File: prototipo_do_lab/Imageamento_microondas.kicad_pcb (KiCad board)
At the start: 4 copper layers, 200 x 150 mm, 121 parts, among them J1 0732511352, J10 0732511352, J11 TB0012-508-03GR, J12 0732511352, J13 0732511352, J2 0732511352, J3 0732511352, J4 0732511352, J5 0732511352, J6 0732511352, J7 0732511352, J8 0732511352, J9 0732511352, U1 SKY13373-460LF, U10 SKY13373-460LF, U11 SKY13373-460LF, U12 SKY13373-460LF, U13 SKY13373-460LF, U14 SKY13373-460LF, U15 SKY13373-460LF, U16 SKY13373-460LF, U17 ESP32-DEVKITC-32E, U18 MCP23016-I_SP, U2 SKY13373-460LF, U3 SKY13373-460LF, U4 SKY13373-460LF, U5 SKY13373-460LF, U6 SKY13373-460LF, U7 SKY13373-460LF, U8 SKY13373-460LF, U9 SKY13373-460LF

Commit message: backup version before new trace tracking
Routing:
- net /arbitragem/I2C_2: track 204.1 -> 0.00 mm
- net /arbitragem/I2C_1: track 165.8 -> 0.00 mm
- net /CE2_2: track 156.1 -> 19.2 mm, vias 1 -> 0
- net /CE1_1: track 144.6 -> 9.79 mm, vias 1 -> 0
- net /CE1_2: track 143.0 -> 8.31 mm, vias 1 -> 0
- net /CE2_1: track 153.8 -> 23.9 mm, vias 1 -> 0
- net /CA_14: track 137.4 -> 10.5 mm, vias 1 -> 0
- net /CA_13: track 142.1 -> 15.6 mm, vias 1 -> 0
- net /CE2_6: track 124.1 -> 8.33 mm, vias 1 -> 0
- net /CE2_5: track 125.1 -> 9.69 mm, vias 1 -> 0
- net /CA_4: track 125.0 -> 12.4 mm, vias 1 -> 0
- net /CA_3: track 123.3 -> 12.0 mm, vias 1 -> 0
- net /CE2_4: track 106.4 -> 8.32 mm, vias 1 -> 0
- net /CA_15: track 109.9 -> 12.0 mm, vias 1 -> 0
- net /CE2_3: track 107.7 -> 9.78 mm, vias 1 -> 0
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- removed copper zone on F.Cu, net GND
- removed copper zone on In1.Cu, net GND
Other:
- copper layers 4 -> 2

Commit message: before moving components
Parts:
- removed TP1, TP10, TP11, TP12, TP13, TP14, TP15, TP16, TP17, TP18, TP19, TP2, TP20, TP21, TP22, TP23, TP24, TP25, TP26, TP27, TP28, TP29, TP3, TP30, TP31, TP32, TP4, TP7, TP8, TP9: TestPoint, TestPoint:TestPoint_Pad_D1.5mm
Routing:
- net (no net): track 0.00 -> 355.1 mm
- net /R2_2: track 97.0 -> 0.00 mm
- net /R2_1: track 96.8 -> 0.00 mm
- net /R2_4: track 96.6 -> 0.00 mm
- net /R2_7: track 96.5 -> 0.00 mm
- net /R2_5: track 96.4 -> 0.00 mm
- net /R2_6: track 95.8 -> 0.00 mm
- net /R1_2: track 92.5 -> 0.00 mm
- net /R1_3: track 86.2 -> 0.00 mm
- net /R1_1: track 84.4 -> 0.00 mm
- net VDD: track 80.0 -> 0.00 mm
- net /segunda_camada_emissao/EXT_E: track 74.6 -> 0.00 mm
- net /E2_6: track 74.5 -> 0.00 mm
- net /E2_7: track 74.5 -> 0.00 mm
- net /E2_3: track 74.5 -> 0.00 mm
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
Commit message: track rounding partially made
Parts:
- removed TP5, TP6: TestPoint, TestPoint:TestPoint_Pad_D1.5mm
- moved C25 9.00 mm to (89.1, 101.2)
- moved C27 9.00 mm to (83.7, 104.9)
- moved C28 9.00 mm to (87.3, 104.9)
- moved C33 9.00 mm to (156.6, 90.5)
- moved C34 9.00 mm to (160.2, 90.5)
- moved C35 9.00 mm to (118.6, 90.3)
- moved C36 9.00 mm to (122.2, 90.3)
- moved C37 9.00 mm to (191.5, 105.0)
- moved C38 9.00 mm to (195.1, 105.0)
- moved C44 9.00 mm to (162.1, 86.8)
- moved C45 9.00 mm to (197.0, 101.2)
- moved C48 9.00 mm to (124.1, 86.6)
- moved R1 9.00 mm to (83.7, 108.3)
- moved R4 9.00 mm to (156.6, 93.9)
- moved R5 9.00 mm to (118.6, 93.7)
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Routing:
- net (no net): track 355.1 -> 1194.9 mm

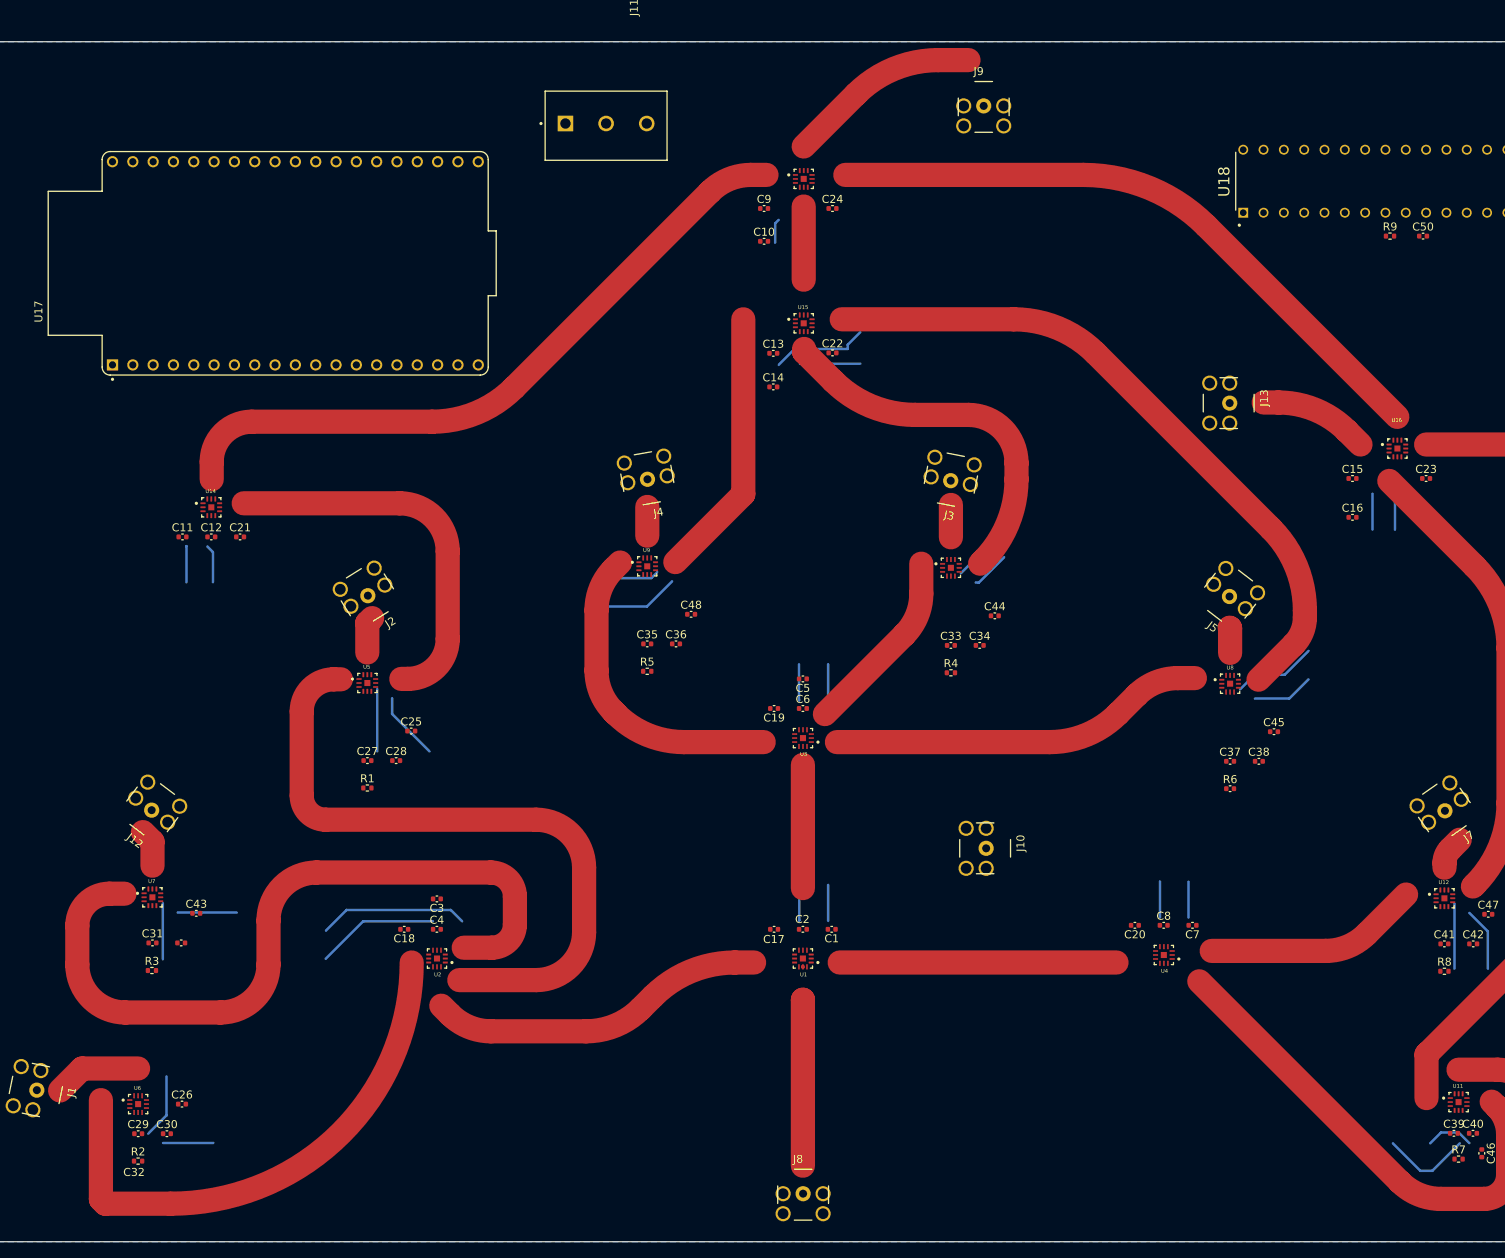
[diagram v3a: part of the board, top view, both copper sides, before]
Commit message: track rounding finished, still need validation
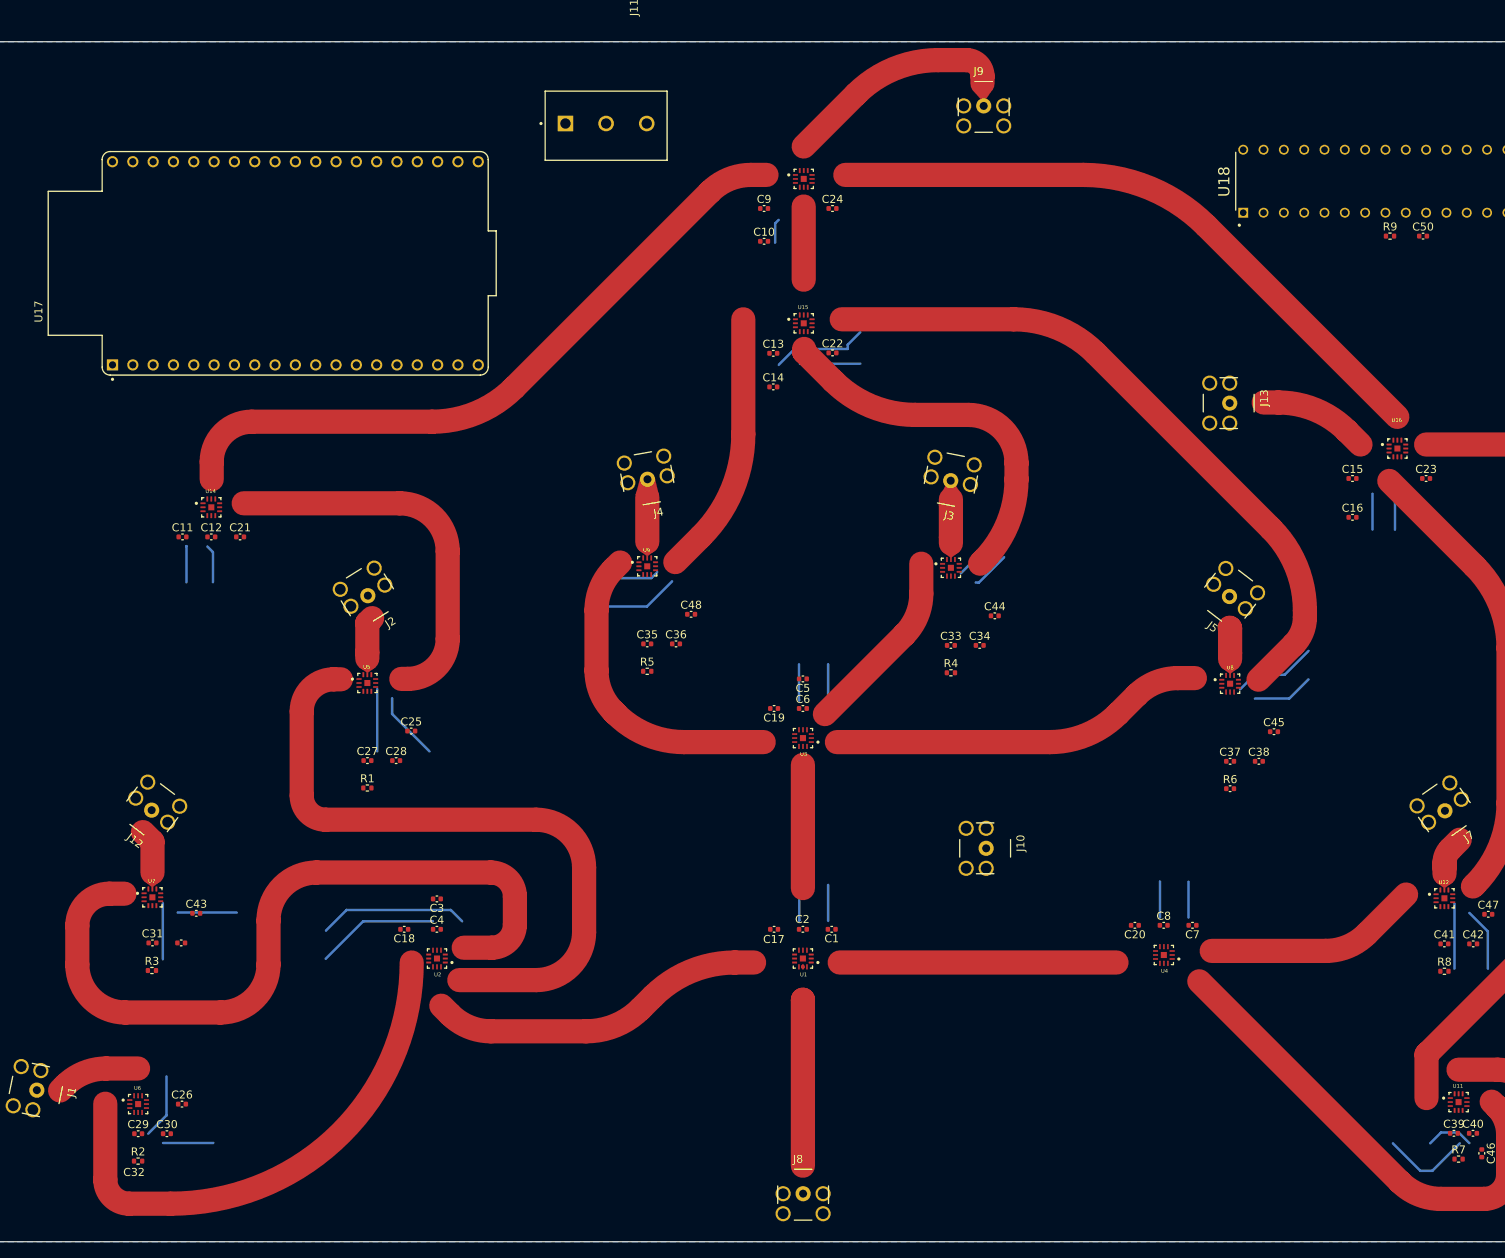
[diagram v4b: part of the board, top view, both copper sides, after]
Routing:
- net (no net): track 1194.9 -> 1143.0 mm
- net Net-(U13-RFC): track 0.00 -> 28.1 mm
- net Net-(U9-RFC): track 0.00 -> 5.55 mm
- net Net-(U7-RFC): track 0.00 -> 5.55 mm
- net Net-(U10-RFC): track 0.00 -> 5.49 mm
- net Net-(U5-RFC): track 0.00 -> 5.29 mm
- net Net-(U12-RFC): track 0.00 -> 4.93 mm
- net Net-(U8-RFC): track 0.00 -> 3.95 mm

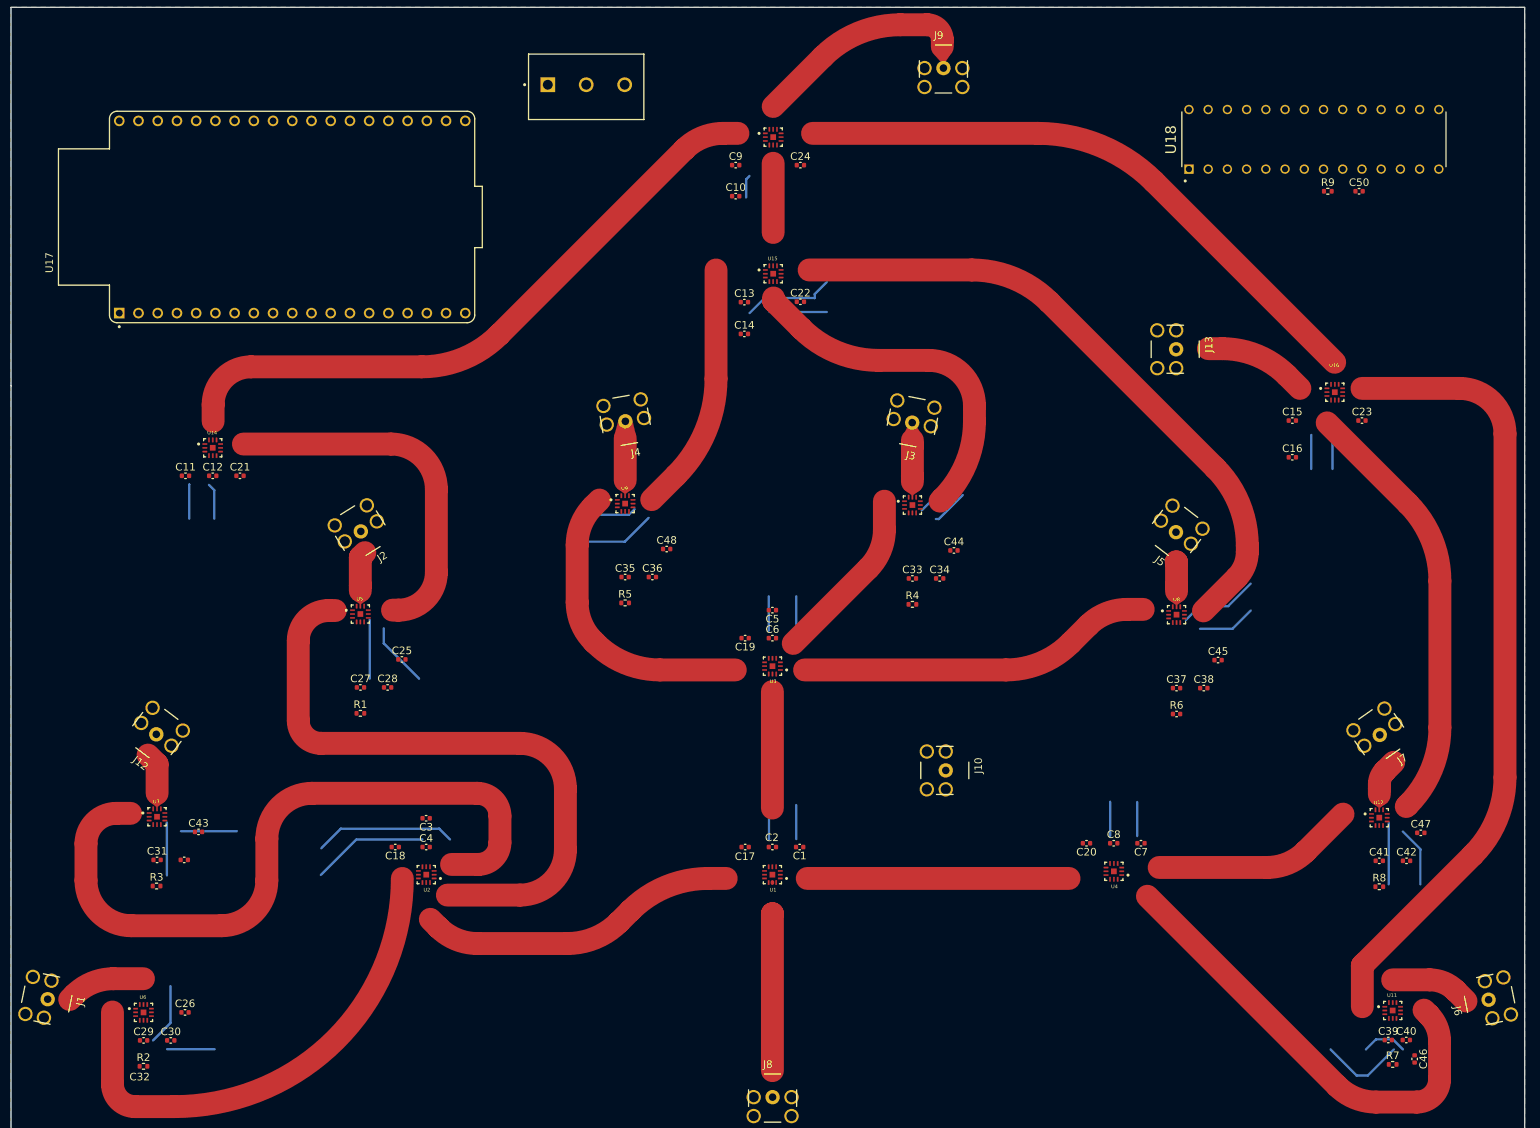
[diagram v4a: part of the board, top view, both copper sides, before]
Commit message: SMA connections finished
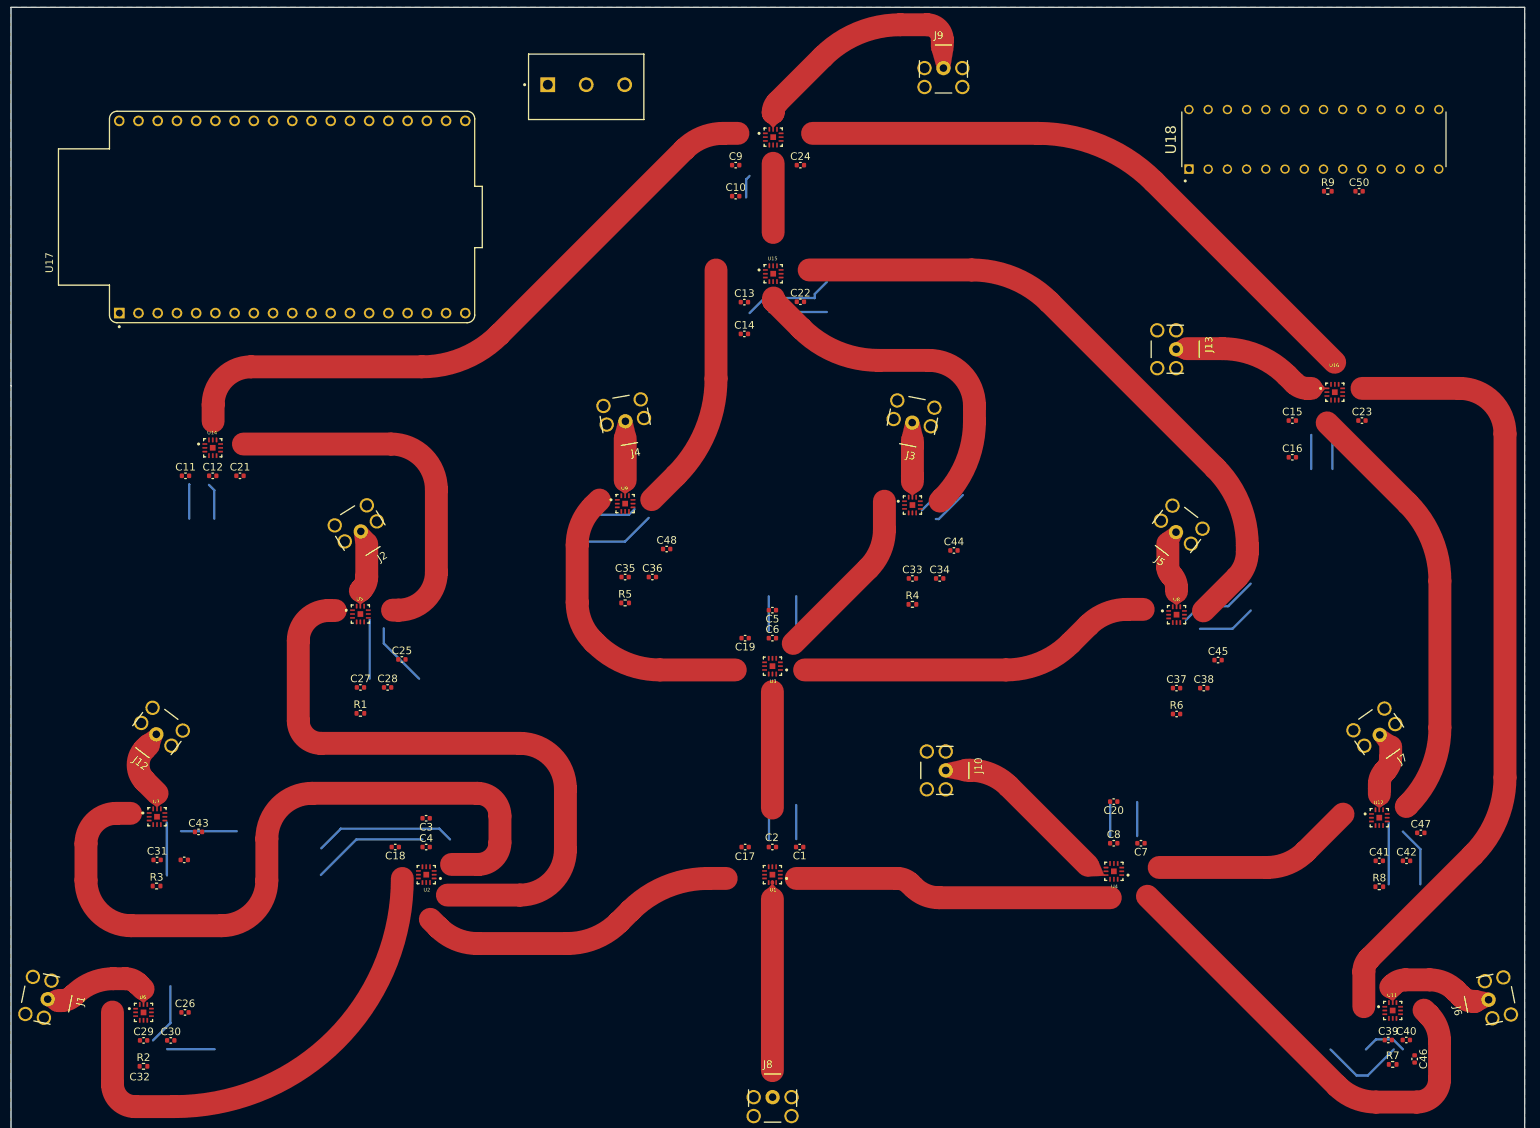
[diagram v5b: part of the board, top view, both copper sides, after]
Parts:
- moved C20 6.57 mm to (183.2, 120.0)
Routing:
- net (no net): track 1143.0 -> 1094.8 mm
- net Net-(U1-RFC): track 0.00 -> 22.7 mm
- net /segunda_camada_emissao/EXT_E: track 0.00 -> 20.9 mm
- net /segunda_camada_recepcao/EXT_R: track 0.00 -> 17.9 mm
- net Net-(U6-RFC): track 0.00 -> 12.4 mm
- net Net-(U11-RFC): track 0.00 -> 12.3 mm
- net Net-(U8-RFC): track 3.95 -> 6.63 mm
- net Net-(U7-RFC): track 5.55 -> 7.57 mm
- net Net-(U12-RFC): track 4.93 -> 6.69 mm
- net Net-(U5-RFC): track 5.29 -> 6.43 mm
- net Net-(U13-RFC): track 28.1 -> 28.8 mm

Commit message: rf tracking finished
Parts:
- moved C11 11.2 mm to (62.6, 88.0)
- moved C2 9.18 mm to (131.2, 120.0)
- moved C12 6.34 mm to (62.6, 83.0)
- moved C21 6.30 mm to (66.4, 83.0)
- moved C31 4.47 mm to (60.8, 129.7)
- moved C32 4.47 mm to (64.4, 129.7)
- moved C41 4.47 mm to (214.3, 129.8)
- moved C42 4.47 mm to (217.9, 129.8)
- moved C47 4.47 mm to (219.8, 126.1)
- moved R3 4.47 mm to (60.7, 133.1)
- moved R8 4.47 mm to (214.3, 133.2)
- moved C43 4.47 mm to (66.3, 126.0)
- moved C26 4.32 mm to (64.8, 148.1)
- moved C1 3.87 mm to (145.4, 124.8)
- moved C17 3.63 mm to (131.2, 124.5)
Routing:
- net (no net): track 1094.8 -> 84.4 mm
- net /R2_7: track 0.00 -> 105.2 mm
- net /R2_2: track 0.00 -> 98.0 mm
- net /R2_4: track 0.00 -> 89.8 mm
- net /R1_1: track 0.00 -> 88.0 mm
- net /R1_3: track 0.00 -> 83.4 mm
- net /E2_1: track 0.00 -> 83.3 mm
- net /E2_2: track 0.00 -> 68.4 mm
- net /E2_7: track 0.00 -> 64.4 mm
- net /R2_8: track 0.00 -> 61.6 mm
- net /R2_3: track 0.00 -> 55.6 mm
- net /R2_6: track 0.00 -> 52.6 mm
- net /E1_1: track 0.00 -> 50.9 mm
- net /R2_1: track 0.00 -> 50.2 mm
- net /E2_4: track 0.00 -> 49.6 mm
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
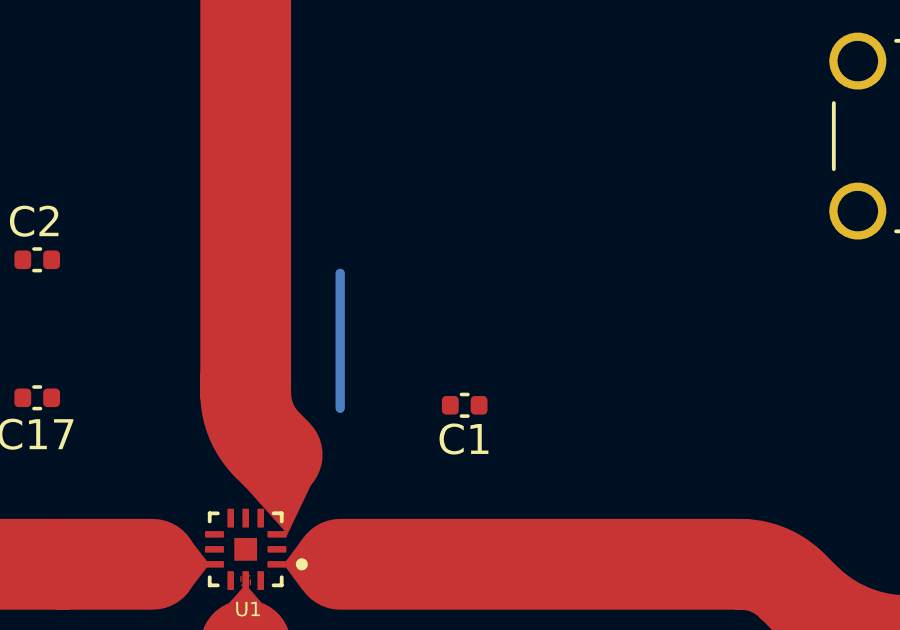
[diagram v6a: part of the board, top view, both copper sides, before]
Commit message: new footprint added to lab prototipe
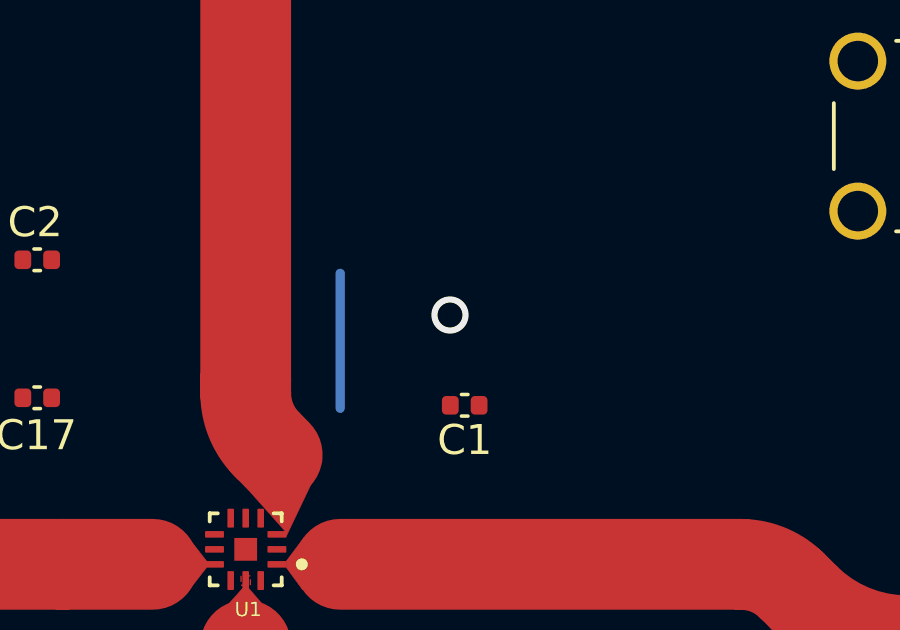
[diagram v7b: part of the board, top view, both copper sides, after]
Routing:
- net (no net): vias 0 -> 1
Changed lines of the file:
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@@
+		(net 0)
+	)
+	(via
+		(at 144.91 121.79)
+		(size 1.243)
+		(drill 0.83)
+		(layers "F.Cu" "B.Cu")
 		(net 0)
 	)

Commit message: footprint uptated in board still needs validation
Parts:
- U1, U10, U11, U12, U13, U14, U15, U16, U2, U3, U4, U5, U6, U7, U8, U9: footprint SKY13373-460LF:QFN50P200X200X65-13N -> SKY13373-460LF:QFN50P200X200X65-13N_1LabProt
